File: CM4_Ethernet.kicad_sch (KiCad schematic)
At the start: 7 parts, among them J1 LPHS-04-16-L-VP1-GP

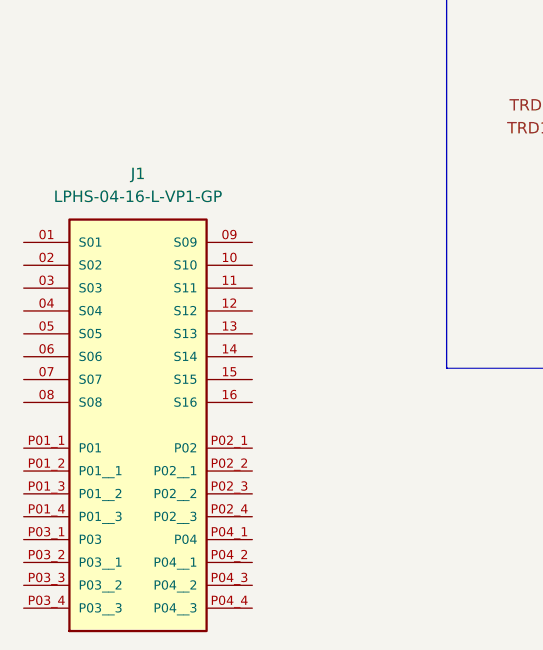
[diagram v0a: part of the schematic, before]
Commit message: Added other LED indicators, ethernet and connector (main connector to other pcb's)
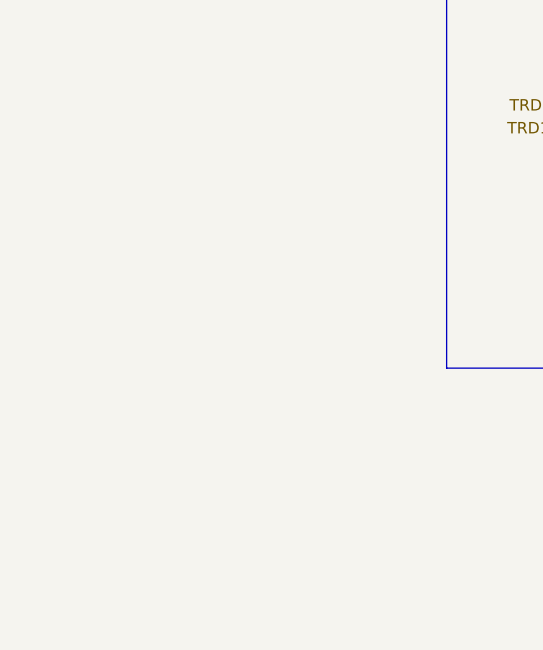
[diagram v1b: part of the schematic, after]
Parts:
- removed J1: LPHS-04-16-L-VP1-GP, dz_con:SAMTEC_LPHS-04-16-X-VP1-GP, symbol #dzdb:s_con/CON-SAMTEC-LPHS-04-16-L-VP1-GP

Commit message: minor changes/cleanup
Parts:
- renumbered D4 to D3, D2 to D4, R2 to R3
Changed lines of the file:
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@@
 		(dnp no)
 		(fields_autoplaced yes)
-		(property "Reference" "#PWR011"
+		(property "Reference" "#PWR013"
 			(at 138.43 63.5 0)
 			(effects
@@
 		)
 		(instances
-			(project ""
-				(path "/ce1819b2-f280-40ed-834f-6fe4d12f809d/c2b6dac3-d6fd-4d5d-bd17-0cff91db88eb/b11889ff-9e53-460e-a5df-2ddc3c461adc/3057b5eb-f1b7-4f0b-8332-d97cb83907a8/9f7bc1e5-4b64-43dc-b368-101a610271ca"
-					(reference "#PWR011")
+			(project "nautilus_mainboard"
+				(path "/ce1819b2-f280-40ed-834f-6fe4d12f809d/c2b6dac3-d6fd-4d5d-bd17-0cff91db88eb/0837dad1-ec16-488a-a684-981e55247089/9f7bc1e5-4b64-43dc-b368-101a610271ca"
+					(reference "#PWR013")
 					(unit 1)
 				)
@@
 		)
 		(instances
-			(project ""
-				(path "/ce1819b2-f280-40ed-834f-6fe4d12f809d/c2b6dac3-d6fd-4d5d-bd17-0cff91db88eb/b11889ff-9e53-460e-a5df-2ddc3c461adc/3057b5eb-f1b7-4f0b-8332-d97cb83907a8/9f7bc1e5-4b64-43dc-b368-101a610271ca"
+			(project "nautilus_mainboard"
+				(path "/ce1819b2-f280-40ed-834f-6fe4d12f809d/c2b6dac3-d6fd-4d5d-bd17-0cff91db88eb/0837dad1-ec16-488a-a684-981e55247089/9f7bc1e5-4b64-43dc-b368-101a610271ca"
 					(reference "TPD4EUSB30DQAR1")
 					(unit 1)
@@
 		(dnp no)
 		(fields_autoplaced yes)
-		(property "Reference" "R2"
+		(property "Reference" "R3"
 			(at 176.53 35.56 90)
 			(effects
@@
 		)
 		(instances
-			(project ""
-				(path "/ce1819b2-f280-40ed-834f-6fe4d12f809d/c2b6dac3-d6fd-4d5d-bd17-0cff91db88eb/b11889ff-9e53-460e-a5df-2ddc3c461adc/3057b5eb-f1b7-4f0b-8332-d97cb83907a8/9f7bc1e5-4b64-43dc-b368-101a610271ca"
-					(reference "R2")
+			(project "nautilus_mainboard"
+				(path "/ce1819b2-f280-40ed-834f-6fe4d12f809d/c2b6dac3-d6fd-4d5d-bd17-0cff91db88eb/0837dad1-ec16-488a-a684-981e55247089/9f7bc1e5-4b64-43dc-b368-101a610271ca"
+					(reference "R3")
 					(unit 1)
 				)
@@
 		(instances
 			(project "nautilus_mainboard"
-				(path "/ce1819b2-f280-40ed-834f-6fe4d12f809d/c2b6dac3-d6fd-4d5d-bd17-0cff91db88eb/b11889ff-9e53-460e-a5df-2ddc3c461adc/3057b5eb-f1b7-4f0b-8332-d97cb83907a8/9f7bc1e5-4b64-43dc-b368-101a610271ca"
+				(path "/ce1819b2-f280-40ed-834f-6fe4d12f809d/c2b6dac3-d6fd-4d5d-bd17-0cff91db88eb/0837dad1-ec16-488a-a684-981e55247089/9f7bc1e5-4b64-43dc-b368-101a610271ca"
 					(reference "R4")
 					(unit 1)
@@
 		(on_board yes)
 		(dnp no)
-		(property "Reference" "D2"
+		(property "Reference" "D4"
 			(at 196.5325 52.07 0)
 			(effects
@@
 		)
 		(instances
-			(project ""
-				(path "/ce1819b2-f280-40ed-834f-6fe4d12f809d/c2b6dac3-d6fd-4d5d-bd17-0cff91db88eb/b11889ff-9e53-460e-a5df-2ddc3c461adc/3057b5eb-f1b7-4f0b-8332-d97cb83907a8/9f7bc1e5-4b64-43dc-b368-101a610271ca"
-					(reference "D2")
+			(project "nautilus_mainboard"
+				(path "/ce1819b2-f280-40ed-834f-6fe4d12f809d/c2b6dac3-d6fd-4d5d-bd17-0cff91db88eb/0837dad1-ec16-488a-a684-981e55247089/9f7bc1e5-4b64-43dc-b368-101a610271ca"
+					(reference "D4")
 					(unit 1)
 				)
@@
 		(dnp no)
 		(fields_autoplaced yes)
-		(property "Reference" "D4"
+		(property "Reference" "D3"
 			(at 192.7225 35.56 0)
 			(effects
@@
 		)
 		(instances
-			(project ""
-				(path "/ce1819b2-f280-40ed-834f-6fe4d12f809d/c2b6dac3-d6fd-4d5d-bd17-0cff91db88eb/b11889ff-9e53-460e-a5df-2ddc3c461adc/3057b5eb-f1b7-4f0b-8332-d97cb83907a8/9f7bc1e5-4b64-43dc-b368-101a610271ca"
-					(reference "D4")
+			(project "nautilus_mainboard"
+				(path "/ce1819b2-f280-40ed-834f-6fe4d12f809d/c2b6dac3-d6fd-4d5d-bd17-0cff91db88eb/0837dad1-ec16-488a-a684-981e55247089/9f7bc1e5-4b64-43dc-b368-101a610271ca"
+					(reference "D3")
 					(unit 1)
 				)
@@
 		(dnp no)
 		(fields_autoplaced yes)
-		(property "Reference" "#PWR012"
+		(property "Reference" "#PWR017"
 			(at 138.43 109.22 0)
 			(effects
@@
 		(instances
 			(project "nautilus_mainboard"
-				(path "/ce1819b2-f280-40ed-834f-6fe4d12f809d/c2b6dac3-d6fd-4d5d-bd17-0cff91db88eb/b11889ff-9e53-460e-a5df-2ddc3c461adc/3057b5eb-f1b7-4f0b-8332-d97cb83907a8/9f7bc1e5-4b64-43dc-b368-101a610271ca"
-					(reference "#PWR012")
+				(path "/ce1819b2-f280-40ed-834f-6fe4d12f809d/c2b6dac3-d6fd-4d5d-bd17-0cff91db88eb/0837dad1-ec16-488a-a684-981e55247089/9f7bc1e5-4b64-43dc-b368-101a610271ca"
+					(reference "#PWR017")
 					(unit 1)
 				)
@@
 		(dnp no)
 		(fields_autoplaced yes)
-		(property "Reference" "#PWR013"
+		(property "Reference" "#PWR018"
 			(at 213.36 46.99 0)
 			(effects
@@
 		)
 		(instances
-			(project ""
-				(path "/ce1819b2-f280-40ed-834f-6fe4d12f809d/c2b6dac3-d6fd-4d5d-bd17-0cff91db88eb/b11889ff-9e53-460e-a5df-2ddc3c461adc/3057b5eb-f1b7-4f0b-8332-d97cb83907a8/9f7bc1e5-4b64-43dc-b368-101a610271ca"
-					(reference "#PWR013")
+			(project "nautilus_mainboard"
+				(path "/ce1819b2-f280-40ed-834f-6fe4d12f809d/c2b6dac3-d6fd-4d5d-bd17-0cff91db88eb/0837dad1-ec16-488a-a684-981e55247089/9f7bc1e5-4b64-43dc-b368-101a610271ca"
+					(reference "#PWR018")
 					(unit 1)
 				)
@@
 		(instances
 			(project "nautilus_mainboard"
-				(path "/ce1819b2-f280-40ed-834f-6fe4d12f809d/c2b6dac3-d6fd-4d5d-bd17-0cff91db88eb/b11889ff-9e53-460e-a5df-2ddc3c461adc/3057b5eb-f1b7-4f0b-8332-d97cb83907a8/9f7bc1e5-4b64-43dc-b368-101a610271ca"
+				(path "/ce1819b2-f280-40ed-834f-6fe4d12f809d/c2b6dac3-d6fd-4d5d-bd17-0cff91db88eb/0837dad1-ec16-488a-a684-981e55247089/9f7bc1e5-4b64-43dc-b368-101a610271ca"
 					(reference "TPD4EUSB30DQAR2")
 					(unit 1)

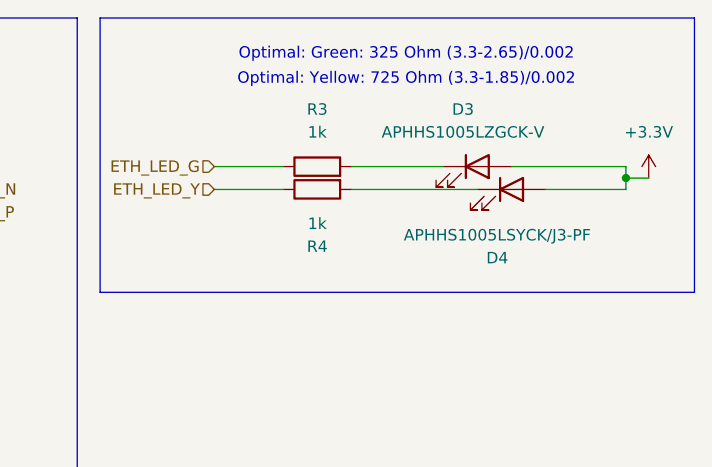
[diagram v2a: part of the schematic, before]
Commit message: added more support for the ssd and fixed LED configuration
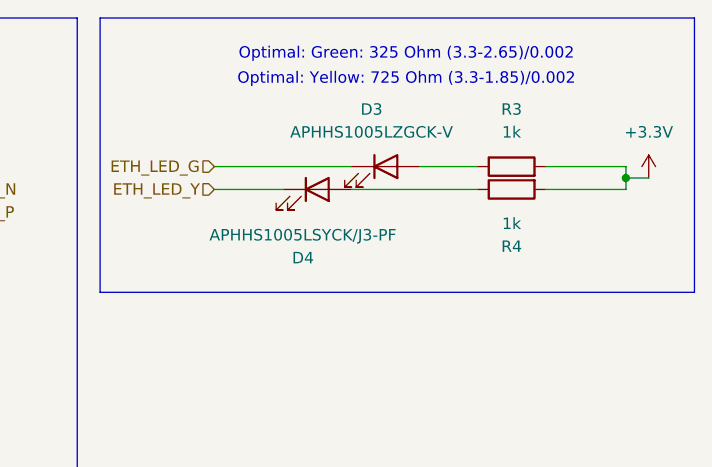
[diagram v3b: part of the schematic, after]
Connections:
- net +3.3V: now also R3.2, R4.2; no longer D3.2 (A), D4.2 (A)
- net ETH_LED_G: now also D3.1 (K); no longer R3.1
- net ETH_LED_Y: now also D4.1 (K); no longer R4.1
- new net: D3.2 (A), R3.1
- new net: D4.2 (A), R4.1
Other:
- moved on the sheet: D3, D4, R3, R4

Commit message: Added Power logic finally. (plus some comments on further improvements)
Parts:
- renumbered D4 to D3, D3 to D4, R3 to R7, R4 to R8
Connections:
- net +3.3V renamed LAN_IN_3.3V
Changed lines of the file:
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@@
 	(rectangle
 		(start 152.4 25.4)
-		(end 218.44 55.88)
+		(end 228.6 55.88)
 		(stroke
 			(width 0)
@@
 			(width 0)
 			(type default)
+		)
+	)
+	(global_label "LAN_IN_3.3V"
+		(shape input)
+		(at 213.36 43.18 0)
+		(fields_autoplaced yes)
+		(effects
+			(font
+				(size 1.27 1.27)
+			)
+			(justify left)
+		)
+		(property "Intersheetrefs" "${INTERSHEET_REFS}"
+			(at 227.7753 43.18 0)
+			(effects
+				(font
+					(size 1.27 1.27)
+				)
+				(justify left)
+				(hide yes)
+			)
 		)
 	)
@@
 		(dnp no)
 		(fields_autoplaced yes)
-		(property "Reference" "#PWR013"
+		(property "Reference" "#PWR019"
 			(at 138.43 63.5 0)
 			(effects
@@
 			(project "nautilus_mainboard"
 				(path "/ce1819b2-f280-40ed-834f-6fe4d12f809d/c2b6dac3-d6fd-4d5d-bd17-0cff91db88eb/0837dad1-ec16-488a-a684-981e55247089/9f7bc1e5-4b64-43dc-b368-101a610271ca"
-					(reference "#PWR013")
+					(reference "#PWR019")
 					(unit 1)
 				)
@@
 		(dnp no)
 		(fields_autoplaced yes)
-		(property "Reference" "R3"
+		(property "Reference" "R7"
 			(at 198.12 35.56 90)
 			(effects
@@
 			(project "nautilus_mainboard"
 				(path "/ce1819b2-f280-40ed-834f-6fe4d12f809d/c2b6dac3-d6fd-4d5d-bd17-0cff91db88eb/0837dad1-ec16-488a-a684-981e55247089/9f7bc1e5-4b64-43dc-b368-101a610271ca"
-					(reference "R3")
+					(reference "R7")
 					(unit 1)
 				)
@@
 		(on_board yes)
 		(dnp no)
-		(property "Reference" "R4"
+		(property "Reference" "R8"
 			(at 198.12 50.8 90)
 			(effects
@@
 			(project "nautilus_mainboard"
 				(path "/ce1819b2-f280-40ed-834f-6fe4d12f809d/c2b6dac3-d6fd-4d5d-bd17-0cff91db88eb/0837dad1-ec16-488a-a684-981e55247089/9f7bc1e5-4b64-43dc-b368-101a610271ca"
-					(reference "R4")
+					(reference "R8")
 					(unit 1)
 				)
@@
 		(on_board yes)
 		(dnp no)
-		(property "Reference" "D4"
+		(property "Reference" "D3"
 			(at 174.9425 52.07 0)
 			(effects
@@
 			(project "nautilus_mainboard"
 				(path "/ce1819b2-f280-40ed-834f-6fe4d12f809d/c2b6dac3-d6fd-4d5d-bd17-0cff91db88eb/0837dad1-ec16-488a-a684-981e55247089/9f7bc1e5-4b64-43dc-b368-101a610271ca"
-					(reference "D4")
+					(reference "D3")
 					(unit 1)
 				)
@@
 		(dnp no)
 		(fields_autoplaced yes)
-		(property "Reference" "D3"
+		(property "Reference" "D4"
 			(at 182.5625 35.56 0)
 			(effects
@@
 			(project "nautilus_mainboard"
 				(path "/ce1819b2-f280-40ed-834f-6fe4d12f809d/c2b6dac3-d6fd-4d5d-bd17-0cff91db88eb/0837dad1-ec16-488a-a684-981e55247089/9f7bc1e5-4b64-43dc-b368-101a610271ca"
-					(reference "D3")
+					(reference "D4")
 					(unit 1)
 				)
@@
 		(dnp no)
 		(fields_autoplaced yes)
-		(property "Reference" "#PWR017"
+		(property "Reference" "#PWR020"
 			(at 138.43 109.22 0)
 			(effects
@@
 			(project "nautilus_mainboard"
 				(path "/ce1819b2-f280-40ed-834f-6fe4d12f809d/c2b6dac3-d6fd-4d5d-bd17-0cff91db88eb/0837dad1-ec16-488a-a684-981e55247089/9f7bc1e5-4b64-43dc-b368-101a610271ca"
-					(reference "#PWR017")
+					(reference "#PWR020")
 					(unit 1)
 				)
-			)
-		)
-	)
-	(symbol
-		(lib_id "power:+3.3V")
-		(at 213.36 43.18 0)
-		(unit 1)
-		(exclude_from_sim no)
-		(in_bom yes)
-		(on_board yes)
-		(dnp no)
-		(fields_autoplaced yes)
-		(property "Reference" "#PWR018"
-			(at 213.36 46.99 0)
-			(effects
-				(font
-					(size 1.27 1.27)
-				)
-				(hide yes)
-			)
-		)
-		(property "Value" "+3.3V"
-			(at 213.36 38.1 0)
-			(effects
-				(font
-					(size 1.27 1.27)
-				)
-			)
-		)
-		(property "Footprint" ""
-			(at 213.36 43.18 0)
-			(effects
-				(font
-					(size 1.27 1.27)
-				)
-				(hide yes)
-			)
-		)
-		(property "Datasheet" ""
-			(at 213.36 43.18 0)
-			(effects
-				(font
-					(size 1.27 1.27)
-				)
-				(hide yes)
-			)
-		)
-		(property "Description" "Power symbol creates a global label with name \"+3.3V\""
-			(at 213.36 43.18 0)
-			(effects
-				(font
-					(size 1.27 1.27)
-				)
-				(hide yes)
-			)
-		)
-		(pin "1"
-		)
-		(instances
-			(project "nautilus_mainboard"
-				(path "/ce1819b2-f280-40ed-834f-6fe4d12f809d/c2b6dac3-d6fd-4d5d-bd17-0cff91db88eb/0837dad1-ec16-488a-a684-981e55247089/9f7bc1e5-4b64-43dc-b368-101a610271ca"
-					(reference "#PWR018")
-					(unit 1)
-				)

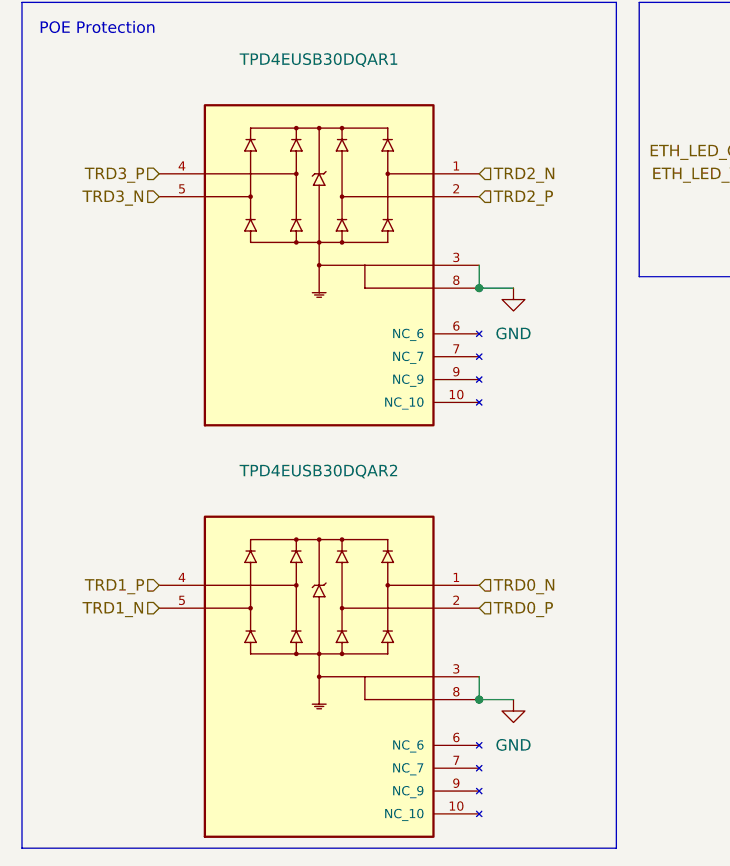
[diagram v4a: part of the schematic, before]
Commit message: multiple changes to the differential pair for easier routing later.
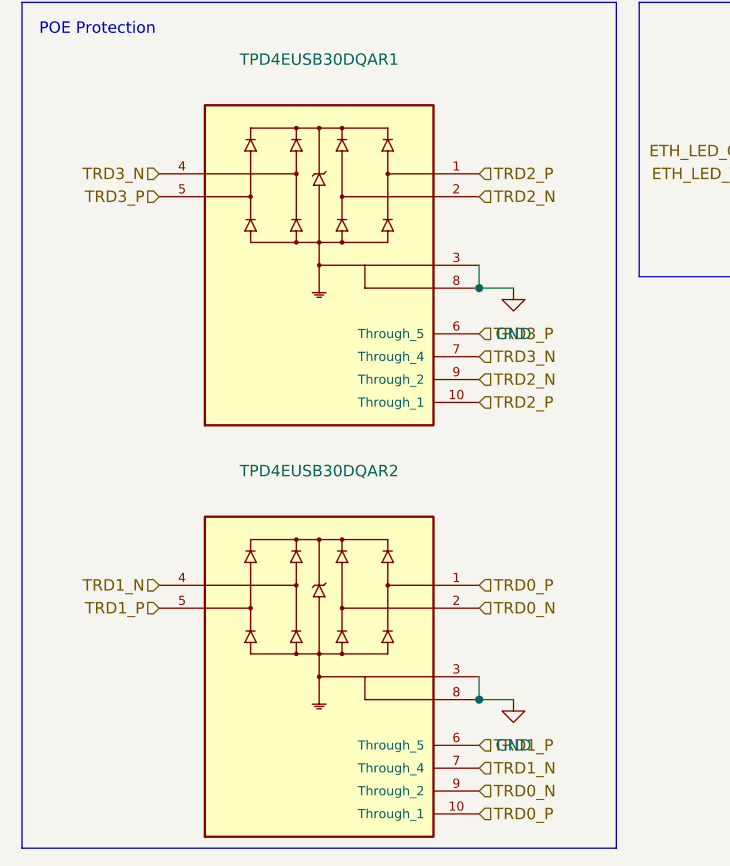
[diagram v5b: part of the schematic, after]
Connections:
- net TRD0_N: now also TPD4EUSB30DQAR2.2, TPD4EUSB30DQAR2.9 (Through_2); no longer TPD4EUSB30DQAR2.1
- net TRD0_P: now also TPD4EUSB30DQAR2.1, TPD4EUSB30DQAR2.10 (Through_1); no longer TPD4EUSB30DQAR2.2
- net TRD1_N: now also TPD4EUSB30DQAR2.4, TPD4EUSB30DQAR2.7 (Through_4); no longer TPD4EUSB30DQAR2.5
- net TRD1_P: now also TPD4EUSB30DQAR2.5, TPD4EUSB30DQAR2.6 (Through_5); no longer TPD4EUSB30DQAR2.4
- net TRD2_N: now also TPD4EUSB30DQAR1.2, TPD4EUSB30DQAR1.9 (Through_2); no longer TPD4EUSB30DQAR1.1
- net TRD2_P: now also TPD4EUSB30DQAR1.1, TPD4EUSB30DQAR1.10 (Through_1); no longer TPD4EUSB30DQAR1.2
- net TRD3_N: now also TPD4EUSB30DQAR1.4, TPD4EUSB30DQAR1.7 (Through_4); no longer TPD4EUSB30DQAR1.5
- net TRD3_P: now also TPD4EUSB30DQAR1.5, TPD4EUSB30DQAR1.6 (Through_5); no longer TPD4EUSB30DQAR1.4
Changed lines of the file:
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@@
+		)
+	)
+	(hierarchical_label "TRD3_P"
+		(shape input)
+		(at 99.06 46.99 180)
+		(effects
+			(font
+				(size 1.27 1.27)
+			)
+			(justify right)
+		)
+	)
+	(hierarchical_label "TRD3_N"
+		(shape input)
+		(at 99.06 44.45 180)
+		(effects
+			(font
+				(size 1.27 1.27)
+			)
+			(justify right)
+		)
+	)
+	(hierarchical_label "TRD3_N"
+		(shape input)
+		(at 134.62 64.77 0)
+		(effects
+			(font
+				(size 1.27 1.27)
+			)
+			(justify left)
+		)
+	)
+	(hierarchical_label "TRD2_P"
+		(shape input)
+		(at 134.62 44.45 0)
+		(effects
+			(font
+				(size 1.27 1.27)
+			)
+			(justify left)
 		)
 	)
 	(hierarchical_label "TRD0_P"
 		(shape input)
+		(at 134.62 90.17 0)
+		(effects
+			(font
+				(size 1.27 1.27)
+			)
+			(justify left)
+		)
+	)
+	(hierarchical_label "TRD1_N"
+		(shape input)
+		(at 99.06 90.17 180)
+		(effects
+			(font
+				(size 1.27 1.27)
+			)
+			(justify right)
+		)
+	)
+	(hierarchical_label "ETH_LED_Y"
+		(shape input)
+		(at 165.1 44.45 180)
+		(effects
+			(font
+				(size 1.27 1.27)
+			)
+			(justify right)
+		)
+	)
+	(hierarchical_label "ETH_LED_G"
+		(shape input)
+		(at 165.1 41.91 180)
+		(effects
+			(font
+				(size 1.27 1.27)
+			)
+			(justify right)
+		)
+	)
+	(hierarchical_label "TRD2_N"
+		(shape input)
+		(at 134.62 67.31 0)
+		(effects
+			(font
+				(size 1.27 1.27)
+			)
+			(justify left)
+		)
+	)
+	(hierarchical_label "TRD2_P"
+		(shape input)
+		(at 134.62 69.85 0)
+		(effects
+			(font
+				(size 1.27 1.27)
+			)
+			(justify left)
+		)
+	)
+	(hierarchical_label "TRD0_N"
+		(shape input)
 		(at 134.62 92.71 0)
 		(effects
@@
 		)
 	)
-	(hierarchical_label "ETH_LED_Y"
-		(shape input)
-		(at 165.1 44.45 180)
-		(effects
-			(font
-				(size 1.27 1.27)
-			)
-			(justify right)
-		)
-	)
-	(hierarchical_label "ETH_LED_G"
-		(shape input)
-		(at 165.1 41.91 180)
-		(effects
-			(font
-				(size 1.27 1.27)
-			)
-			(justify right)
-		)
-	)
-	(hierarchical_label "TRD2_P"
+	(hierarchical_label "TRD0_P"
+		(shape input)
+		(at 134.62 115.57 0)
+		(effects
+			(font
+				(size 1.27 1.27)
+			)
+			(justify left)
+		)
+	)
+	(hierarchical_label "TRD2_N"
 		(shape input)
 		(at 134.62 46.99 0)
@@
 		)
 	)
-	(hierarchical_label "TRD2_N"
-		(shape input)
-		(at 134.62 44.45 0)
+	(hierarchical_label "TRD1_N"
+		(shape input)
+		(at 134.62 110.49 0)
 		(effects
 			(font
@@
 	(hierarchical_label "TRD1_P"
 		(shape input)
-		(at 99.06 90.17 180)
-		(effects
-			(font
-				(size 1.27 1.27)
-			)
-			(justify right)
-		)
-	)
-	(hierarchical_label "TRD1_N"
-		(shape input)
 		(at 99.06 92.71 180)
 		(effects
@@
 		)
 	)
-	(hierarchical_label "TRD3_N"
-		(shape input)
-		(at 99.06 46.99 180)
-		(effects
-			(font
-				(size 1.27 1.27)
-			)
-			(justify right)
+	(hierarchical_label "TRD3_P"
+		(shape input)
+		(at 134.62 62.23 0)
+		(effects
+			(font
+				(size 1.27 1.27)
+			)
+			(justify left)
 		)
 	)
 	(hierarchical_label "TRD0_N"
 		(shape input)
-		(at 134.62 90.17 0)
-		(effects
-			(font
-				(size 1.27 1.27)
-			)
-			(justify left)
-		)
-	)
-	(hierarchical_label "TRD3_P"
-		(shape input)
-		(at 99.06 44.45 180)
-		(effects
-			(font
-				(size 1.27 1.27)
-			)
-			(justify right)
+		(at 134.62 113.03 0)
+		(effects
+			(font
+				(size 1.27 1.27)
+			)
+			(justify left)
+		)
+	)
+	(hierarchical_label "TRD1_P"
+		(shape input)
+		(at 134.62 107.95 0)
+		(effects
+			(font
+				(size 1.27 1.27)
+			)
+			(justify left)
 		)
 	)
@@
 	)
 	(symbol
+		(lib_name "s_misc/IC-ESD-TPD4EUSB30_1")
 		(lib_id "#dzdb:s_misc/IC-ESD-TPD4EUSB30")
 		(at 116.84 54.61 0)
